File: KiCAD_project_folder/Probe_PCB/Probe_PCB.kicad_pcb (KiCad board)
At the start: 2 copper layers, 50.8 x 50.8 mm, 10 parts, among them U1 LTC2452ITS8-TRMPBF, U2 BMI160

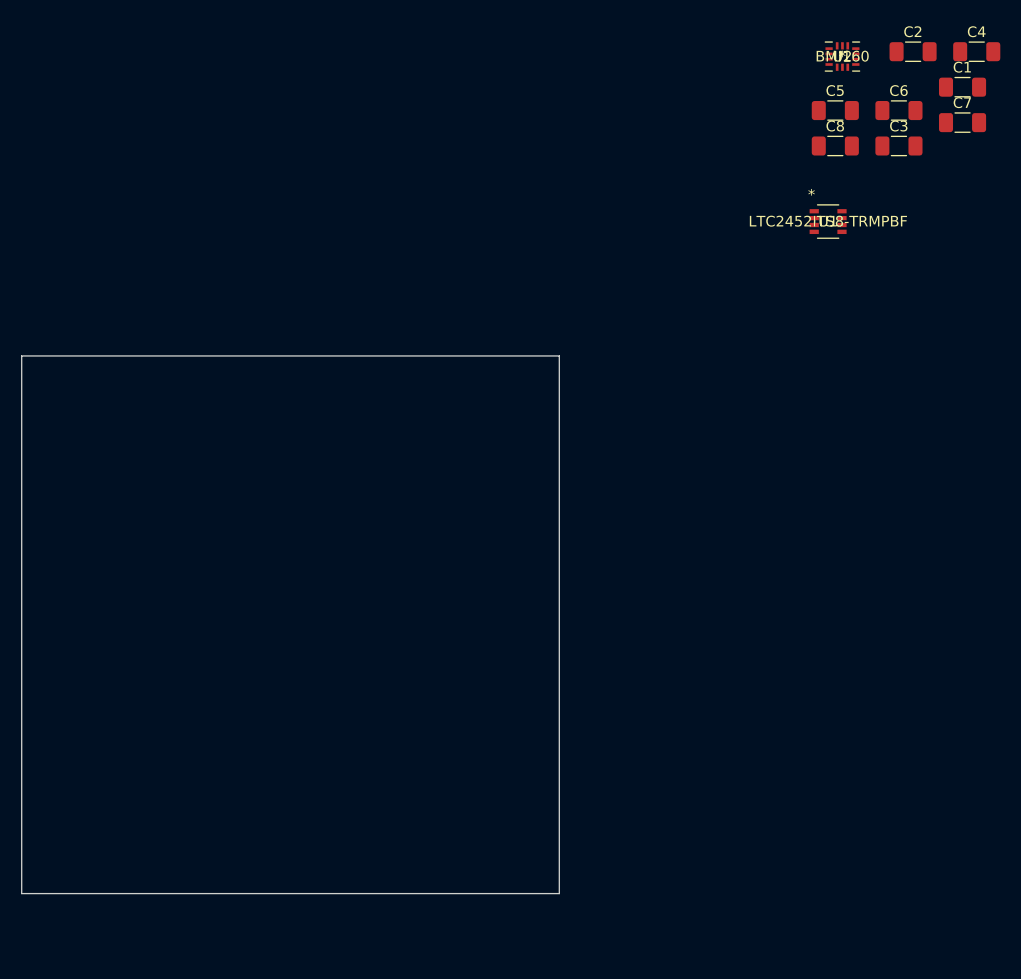
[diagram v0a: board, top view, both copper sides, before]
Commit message: Added draft PCB layout for probe
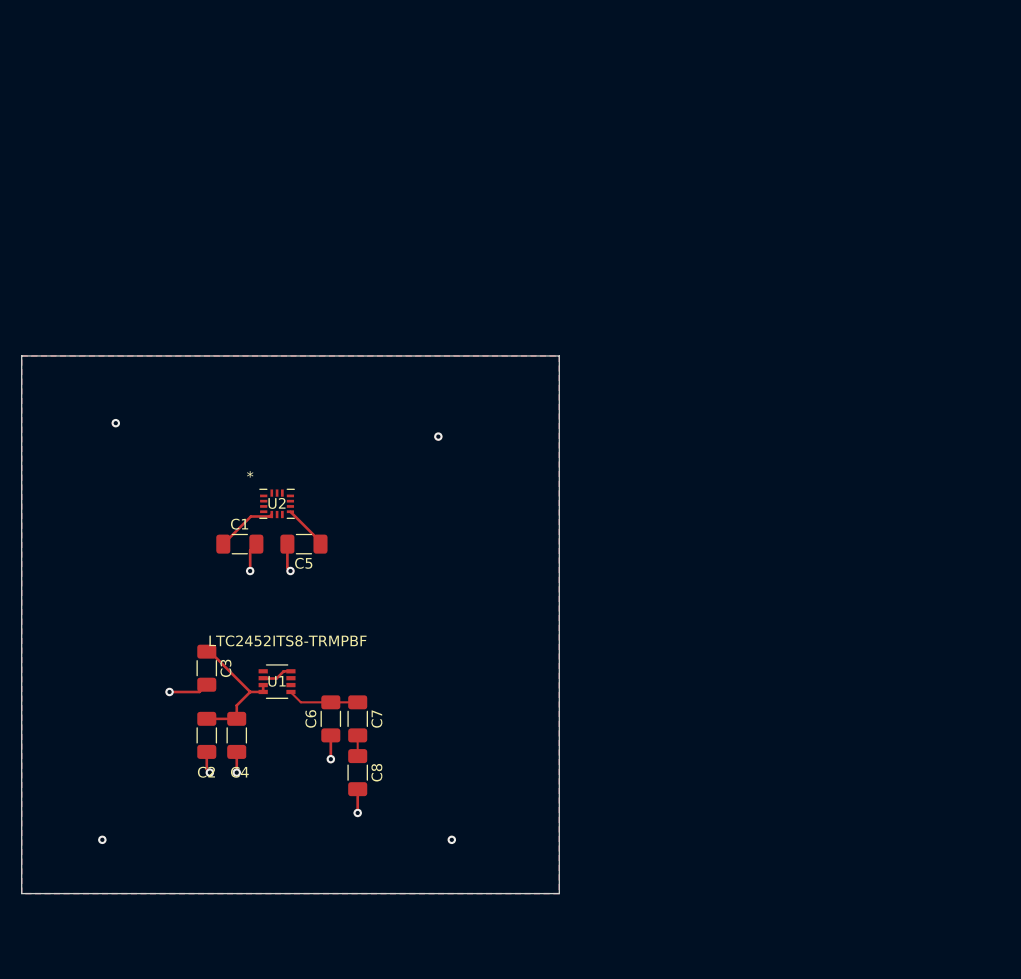
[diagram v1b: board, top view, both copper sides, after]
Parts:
- moved C4 95.2 mm to (134.6, 99.4), turned to -90 degrees
- moved C2 92.9 mm to (131.8, 99.4), turned to -90 degrees
- moved C3 81.9 mm to (131.8, 93.0), turned to -90 degrees
- moved C1 80.8 mm to (134.9, 81.3)
- moved C7 80.3 mm to (146.1, 97.8), turned to -90 degrees
- moved C6 78.6 mm to (143.5, 97.8), turned to 90 degrees
- moved C8 74.4 mm to (146.1, 102.9), turned to -90 degrees
- moved U2 68.1 mm to (138.4, 77.5)
- moved U1 67.8 mm to (138.4, 94.3)
- moved C5 64.8 mm to (141.0, 81.3), turned to 180 degrees
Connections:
- net +3V3 renamed REF
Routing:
- net GNDREF: track 0.00 -> 20.7 mm, vias 0 -> 11
- net REF: track 0.00 -> 13.5 mm
- net /Inertia Measurement Unit & ADC/sense_+: track 0.00 -> 6.75 mm
- net VDDA: track 0.00 -> 5.74 mm
- net VDD: track 0.00 -> 4.24 mm
- net /Inertia Measurement Unit & ADC/sense_-: track 0.00 -> 1.95 mm
- added copper zone on B.Cu, net GNDREF
- added copper zone on F.Cu, net GNDREF
- added copper zone on In1.Cu, net GNDREF
- added copper zone on In2.Cu, net VDD
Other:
- copper layers 2 -> 4

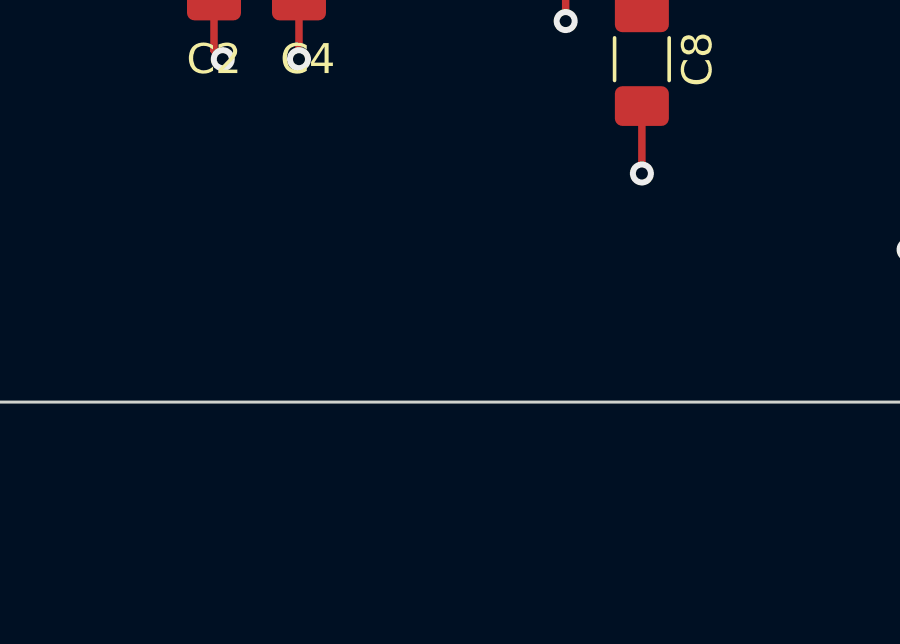
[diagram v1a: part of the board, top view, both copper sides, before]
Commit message: Added connector for probe, needs to be routed
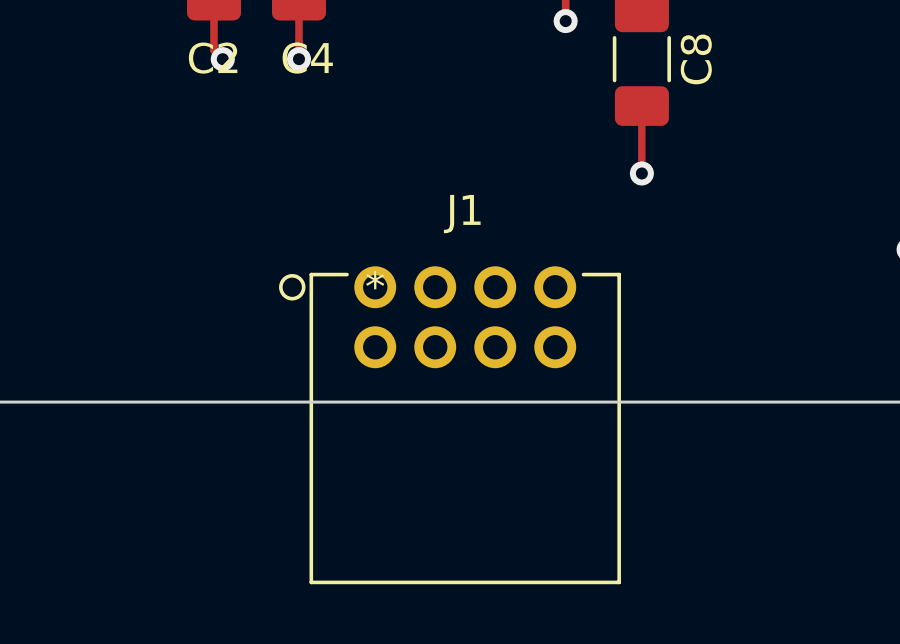
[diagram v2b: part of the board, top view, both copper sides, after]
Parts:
- added J1: DF11-8DP-2DS52, DF11-8POS:DF11-8DP-2DS52, F.Cu at (137.2, 110.5)
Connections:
- net REF renamed +3V3
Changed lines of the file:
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@@
   (net 1 "VDDA")
   (net 2 "GNDREF")
-  (net 3 "REF")
+  (net 3 "+3V3")
   (net 4 "VDD")
   (net 5 "/Inertia Measurement Unit & ADC/sense_+")
@@
   (net 17 "/Inertia Measurement Unit & ADC/~{CS}")
   (net 18 "/Inertia Measurement Unit & ADC/SDO")
+  (footprint "DF11-8POS:DF11-8DP-2DS52" (layer "F.Cu")
+    (at 137.162001 110.4724 180)
+    (property "Sheetfile" "untitled.kicad_sch")
+    (property "Sheetname" "Inertia Measurement Unit & ADC")
+    (attr through_hole)
+    (fp_text reference "J1" (at -2.999999 2.54) (layer "F.SilkS")
+      (effects (font (size 1 1) (thickness 0.15)))
+    )
+    (fp_text value "DF11-8DP-2DS52" (at -2.54 -12.7) (layer "F.SilkS") hide
+      (effects (font (size 1 1) (thickness 0.15)))
+    )
+    (fp_text user "*" (at 0 0) (layer "F.SilkS")
+      (effects (font (size 1 1) (thickness 0.15)))
+    )
+    (fp_text user "Copyright 2021 Accelerated Designs. All rights reserved." (at 0 0) (layer "Cmts.User")
+      (effects (font (size 0.127 0.127) (thickness 0.002)))
+    )
+    (fp_text user "*" (at 0 0) (layer "F.Fab")
+      (effects (font (size 1 1) (thickness 0.15)))
+    )
+    (fp_circle (center 2.765801 0) (end 3.146801 0) (layer "B.SilkS") (width 0.12) (fill none))
+    (fp_line (start -8.130799 -9.8392) (end -8.130799 0.4224) (layer "F.SilkS") (width 0.12))
+    (fp_line (start 0.940763 0.4224) (end 2.130801 0.4224) (layer "F.SilkS") (width 0.12))
+    (fp_line (start -8.130799 0.4224) (end -6.940761 0.4224) (layer "F.SilkS") (width 0.12))
+    (fp_line (start 2.130801 -9.8392) (end -8.130799 -9.8392) (layer "F.SilkS") (width 0.12))
+    (fp_line (start 2.130801 0.4224) (end 2.130801 -9.8392) (layer "F.SilkS") (width 0.12))
+    (fp_circle (center 2.765801 0) (end 3.146801 0) (layer "F.SilkS") (width 0.12) (fill none))
+    (fp_line (start 2.257801 -9.9662) (end -8.257799 -9.9662) (layer "F.CrtYd") (width 0.05))
+    (fp_line (start 2.257801 -9.9662) (end -8.257799 -9.9662) (layer "F.CrtYd") (width 0.05))
+    (fp_line (start -8.257799 -9.9662) (end -8.257799 0.9525) (layer "F.CrtYd") (width 0.05))
+    (fp_line (start -8.257799 -9.9662) (end -8.257799 0.9525) (layer "F.CrtYd") (width 0.05))
+    (fp_line (start -8.257799 0.9525) (end 2.257801 0.9525) (layer "F.CrtYd") (width 0.05))
+    (fp_line (start 2.257801 0.9525) (end 2.257801 -9.9662) (layer "F.CrtYd") (width 0.05))
+    (fp_line (start -8.257799 0.9525) (end 2.257801 0.9525) (layer "F.CrtYd") (width 0.05))
+    (fp_line (start 2.257801 0.9525) (end 2.257801 -9.9662) (layer "F.CrtYd") (width 0.05))
+    (fp_line (start -8.003799 0.2954) (end 2.003801 0.2954) (layer "F.Fab") (width 0.1))
+    (fp_line (start 2.003801 -9.7122) (end -8.003799 -9.7122) (layer "F.Fab") (width 0.1))
+    (fp_line (start 2.003801 0.2954) (end 2.003801 -9.7122) (layer "F.Fab") (width 0.1))
+    (fp_line (start -8.003799 -9.7122) (end -8.003799 0.2954) (layer "F.Fab") (width 0.1))
+    (fp_circle (center 0 1.905) (end 0.381 1.905) (layer "F.Fab") (width 0.1) (fill none))
+    (pad "1" thru_hole circle (at 0 0.000001 180) (size 1.397 1.397) (drill 0.8128) (layers *.Cu *.Mask)
+      (net 16 "/Inertia Measurement Unit & ADC/SDA") (pinfunction "1") (pintype "unspecified"))
+    (pad "2" thru_hole circle (at 0 -2.000001 180) (size 1.397 1.397) (drill 0.8128) (layers *.Cu *.Mask)
+      (net 15 "/Inertia Measurement Unit & ADC/SCK") (pinfunction "2") (pintype "unspecified"))
+    (pad "3" thru_hole circle (at -1.999999 0.000001 180) (size 1.397 1.397) (drill 0.8128) (layers *.Cu *.Mask)
+      (net 14 "/Inertia Measurement Unit & ADC/CSB") (pinfunction "3") (pintype "unspecified"))
+    (pad "4" thru_hole circle (at -1.999999 -2.000001 180) (size 1.397 1.397) (drill 0.8128) (layers *.Cu *.Mask)
+      (net 18 "/Inertia Measurement Unit & ADC/SDO") (pinfunction "4") (pintype "unspecified"))
+    (pad "5" thru_hole circle (at -4 0.000001 180) (size 1.397 1.397) (drill 0.8128) (layers *.Cu *.Mask)
+      (net 17 "/Inertia Measurement Unit & ADC/~{CS}") (pinfunction "5") (pintype "unspecified"))
+    (pad "6" thru_hole circle (at -4 -2.000001 180) (size 1.397 1.397) (drill 0.8128) (layers *.Cu *.Mask)
+      (net 10 "/Inertia Measurement Unit & ADC/INT1") (pinfunction "6") (pintype "unspecified"))
+    (pad "7" thru_hole circle (at -5.999998 0.000001 180) (size 1.397 1.397) (drill 0.8128) (layers *.Cu *.Mask)
+      (net 11 "/Inertia Measurement Unit & ADC/INT2") (pinfunction "7") (pintype "unspecified"))
+    (pad "8" thru_hole circle (at -5.999998 -2.000001 180) (size 1.397 1.397) (drill 0.8128) (layers *.Cu *.Mask)
+      (net 2 "GNDREF") (pinfunction "8") (pintype "unspecified"))
+  )
   (footprint "Capacitor_SMD:C_1206_3216Metric_Pad1.33x1.80mm_HandSolder" (layer "F.Cu")
     (at 143.51 97.79 90)
@@
     (fp_line (start -1.6 0.8) (end -1.6 -0.8) (layer "F.Fab") (width 0.1))
     (pad "1" smd roundrect (at -1.5625 0 270) (size 1.325 1.8) (layers "F.Cu" "F.Paste" "F.Mask") (roundrect_rratio 0.188679)
-      (net 3 "REF") (pintype "passive"))
+      (net 3 "+3V3") (pintype "passive"))
     (pad "2" smd roundrect (at 1.5625 0 270) (size 1.325 1.8) (layers "F.Cu" "F.Paste" "F.Mask") (roundrect_rratio 0.188679)
       (net 2 "GNDREF") (pintype "passive"))
@@
     (fp_line (start -1.6 0.8) (end -1.6 -0.8) (layer "F.Fab") (width 0.1))
     (pad "1" smd roundrect (at -1.5625 0 270) (size 1.325 1.8) (layers "F.Cu" "F.Paste" "F.Mask") (roundrect_rratio 0.188679)
-      (net 3 "REF") (pintype "passive"))
+      (net 3 "+3V3") (pintype "passive"))
     (pad "2" smd roundrect (at 1.5625 0 270) (size 1.325 1.8) (layers "F.Cu" "F.Paste" "F.Mask") (roundrect_rratio 0.188679)
       (net 2 "GNDREF") (pintype "passive"))
@@
     (fp_line (start -1.6 0.8) (end -1.6 -0.8) (layer "F.Fab") (width 0.1))
     (pad "1" smd roundrect (at -1.5625 0 270) (size 1.325 1.8) (layers "F.Cu" "F.Paste" "F.Mask") (roundrect_rratio 0.188679)
-      (net 3 "REF") (pintype "passive"))
+      (net 3 "+3V3") (pintype "passive"))
     (pad "2" smd roundrect (at 1.5625 0 270) (size 1.325 1.8) (layers "F.Cu" "F.Paste" "F.Mask") (roundrect_rratio 0.188679)
       (net 2 "GNDREF") (pintype "passive"))
@@
       (net 2 "GNDREF") (pinfunction "GND") (pintype "power_in"))
     (pad "3" smd rect (at -1.311651 0.325001) (size 0.870699 0.4056) (layers "F.Cu" "F.Paste" "F.Mask")
-      (net 3 "REF") (pinfunction "REF") (pintype "input"))
+      (net 3 "+3V3") (pinfunction "REF") (pintype "input"))
     (pad "4" smd rect (at -1.311651 0.974999) (size 0.870699 0.4056) (layers "F.Cu" "F.Paste" "F.Mask")
-      (net 3 "REF") (pinfunction "VCC") (pintype "power_in"))
+      (net 3 "+3V3") (pinfunction "VCC") (pintype "power_in"))
     (pad "5" smd rect (at 1.311651 0.974999) (size 0.870699 0.4056) (layers "F.Cu" "F.Paste" "F.Mask")
       (net 5 "/Inertia Measurement Unit & ADC/sense_+") (pinfunction "IN-") (pintype "input"))

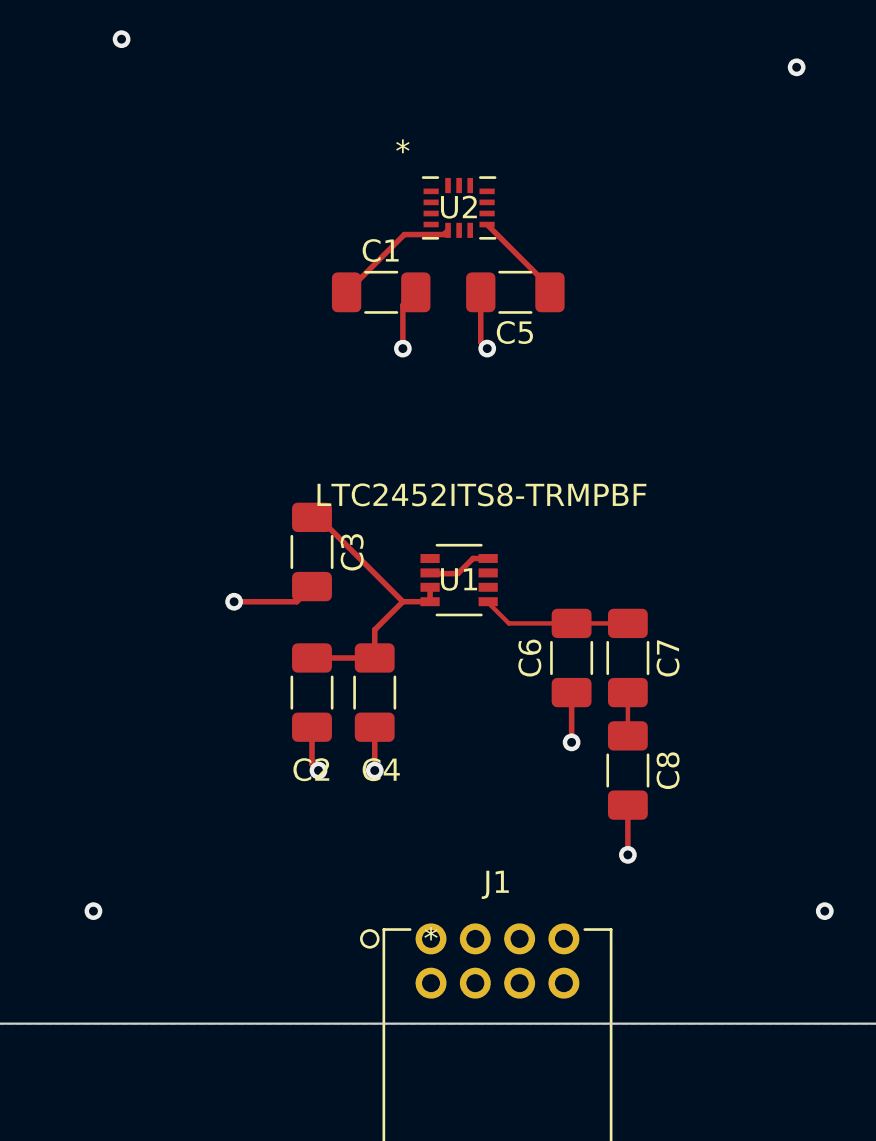
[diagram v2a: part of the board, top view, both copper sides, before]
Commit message: PCB probe modified
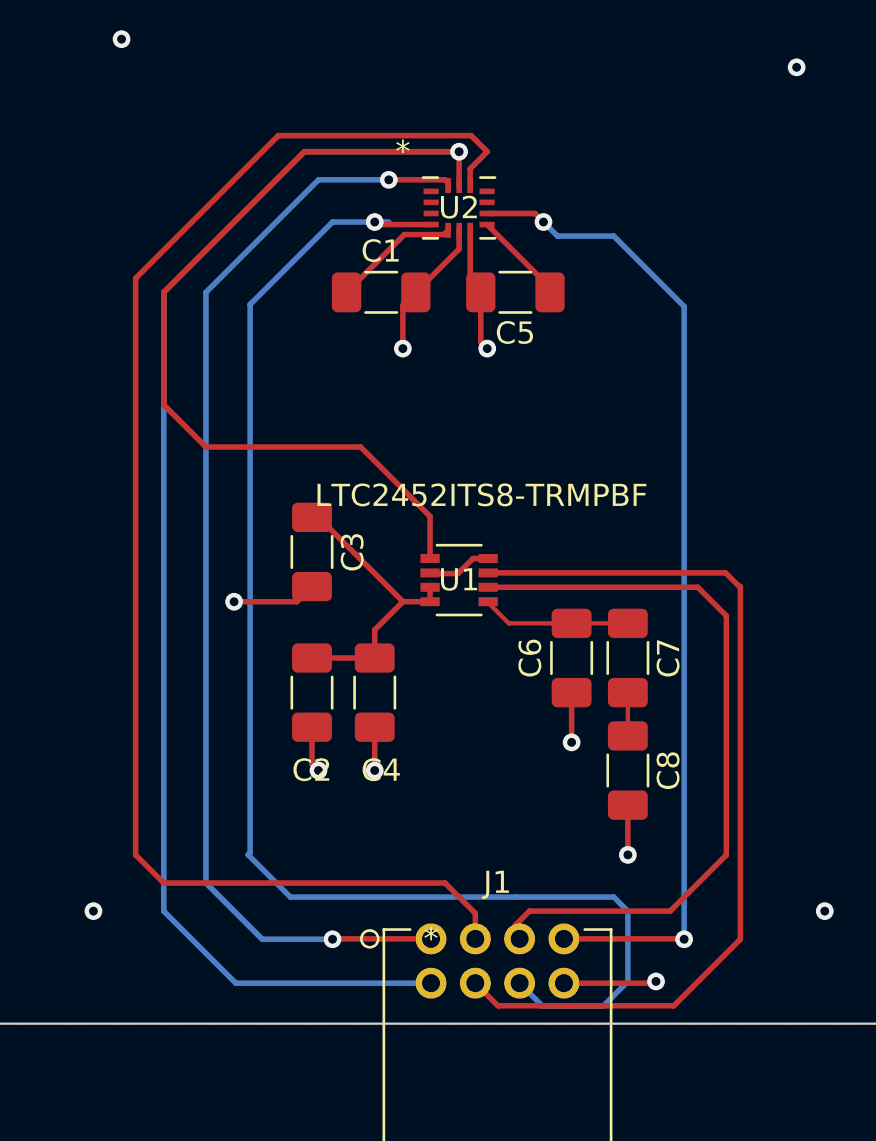
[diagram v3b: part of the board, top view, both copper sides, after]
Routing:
- net /Inertia Measurement Unit & ADC/SCK: track 0.00 -> 95.9 mm, vias 0 -> 1
- net /Inertia Measurement Unit & ADC/CSB: track 0.00 -> 64.4 mm
- net /Inertia Measurement Unit & ADC/INT1: track 0.00 -> 62.4 mm, vias 0 -> 1
- net /Inertia Measurement Unit & ADC/SDA: track 0.00 -> 51.1 mm, vias 0 -> 2
- net /Inertia Measurement Unit & ADC/INT2: track 0.00 -> 44.6 mm, vias 0 -> 2
- net /Inertia Measurement Unit & ADC/SDO: track 0.00 -> 41.2 mm
- net /Inertia Measurement Unit & ADC/~{CS}: track 0.00 -> 33.6 mm
- net GNDREF: track 20.7 -> 31.5 mm, vias 11 -> 12
